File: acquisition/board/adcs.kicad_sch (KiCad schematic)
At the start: 107 parts, among them U1 AD9251, U2 XC7A50T-1FTG256C, U3 AD9251, U4 AD9251, U5 AD9251, U6 ICE40UP5K_QFN48

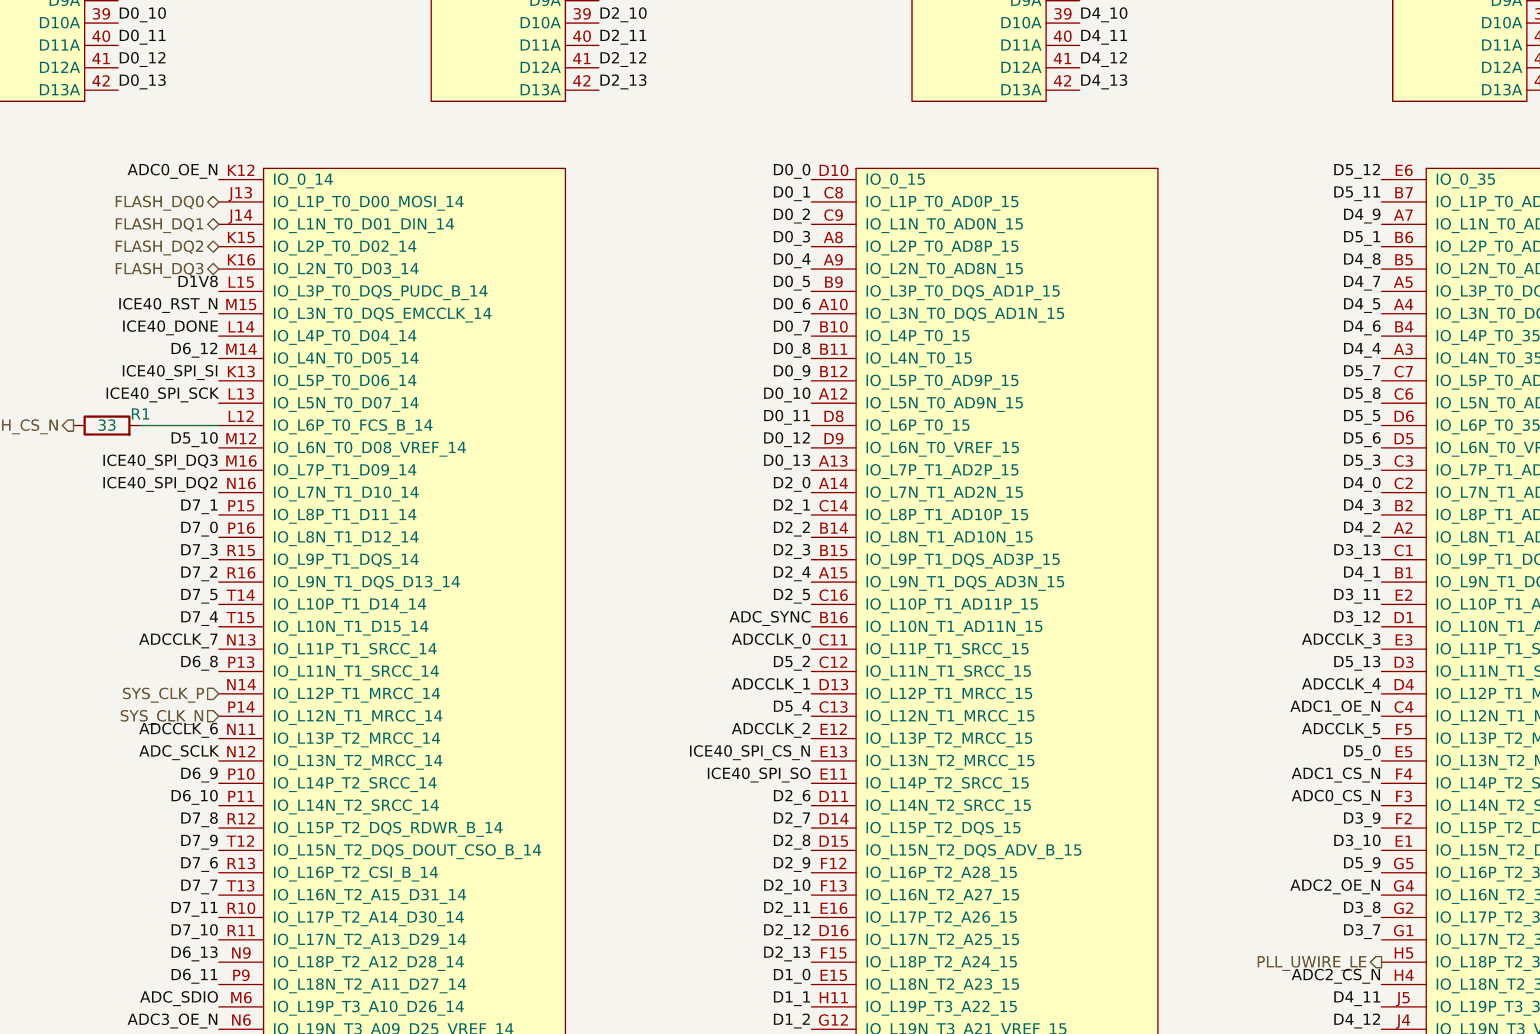
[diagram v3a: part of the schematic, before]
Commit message: Routed most of third ADC data bus
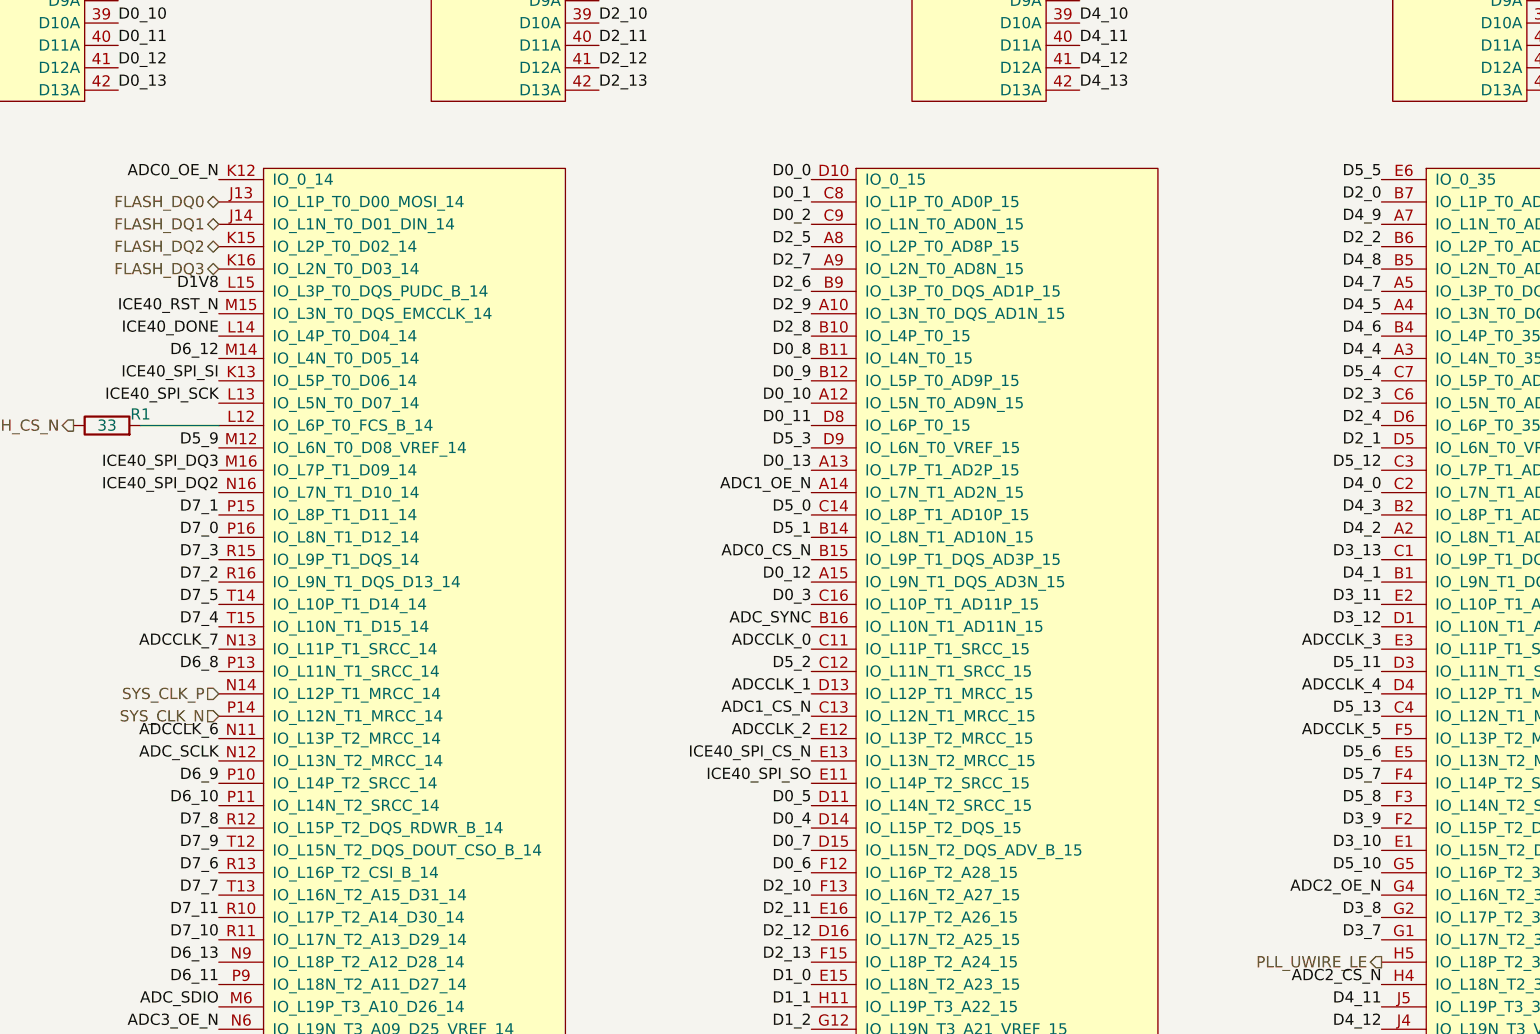
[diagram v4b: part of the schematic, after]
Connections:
- net ADC0_CS_N: now also U2.B15 (IO_L9P_T1_DQS_AD3P_15); no longer U2.F3 (IO_L14N_T2_SRCC_35)
- net ADC1_CS_N: now also U2.C13 (IO_L12N_T1_MRCC_15); no longer U2.F4 (IO_L14P_T2_SRCC_35)
- net ADC1_OE_N: now also U2.A14 (IO_L7N_T1_AD2N_15); no longer U2.C4 (IO_L12N_T1_MRCC_35)
- net D0_12: now also U2.A15 (IO_L9N_T1_DQS_AD3N_15); no longer U2.D9 (IO_L6N_T0_VREF_15)
- net D0_3: now also U2.C16 (IO_L10P_T1_AD11P_15); no longer U2.A8 (IO_L2P_T0_AD8P_15)
- net D0_4: now also U2.D14 (IO_L15P_T2_DQS_15); no longer U2.A9 (IO_L2N_T0_AD8N_15)
- net D0_5: now also U2.D11 (IO_L14N_T2_SRCC_15); no longer U2.B9 (IO_L3P_T0_DQS_AD1P_15)
- net D0_6: now also U2.F12 (IO_L16P_T2_A28_15); no longer U2.A10 (IO_L3N_T0_DQS_AD1N_15)
- net D0_7: now also U2.D15 (IO_L15N_T2_DQS_ADV_B_15); no longer U2.B10 (IO_L4P_T0_15)
- net D2_0: now also U2.B7 (IO_L1P_T0_AD4P_35); no longer U2.A14 (IO_L7N_T1_AD2N_15)
- net D2_1: now also U2.D5 (IO_L6N_T0_VREF_35); no longer U2.C14 (IO_L8P_T1_AD10P_15)
- net D2_2: now also U2.B6 (IO_L2P_T0_AD12P_35); no longer U2.B14 (IO_L8N_T1_AD10N_15)
- net D2_3: now also U2.C6 (IO_L5N_T0_AD13N_35); no longer U2.B15 (IO_L9P_T1_DQS_AD3P_15)
- net D2_4: now also U2.D6 (IO_L6P_T0_35); no longer U2.A15 (IO_L9N_T1_DQS_AD3N_15)
- net D2_5: now also U2.A8 (IO_L2P_T0_AD8P_15); no longer U2.C16 (IO_L10P_T1_AD11P_15)
- net D2_6: now also U2.B9 (IO_L3P_T0_DQS_AD1P_15); no longer U2.D11 (IO_L14N_T2_SRCC_15)
- net D2_7: now also U2.A9 (IO_L2N_T0_AD8N_15); no longer U2.D14 (IO_L15P_T2_DQS_15)
- net D2_8: now also U2.B10 (IO_L4P_T0_15); no longer U2.D15 (IO_L15N_T2_DQS_ADV_B_15)
- net D2_9: now also U2.A10 (IO_L3N_T0_DQS_AD1N_15); no longer U2.F12 (IO_L16P_T2_A28_15)
- net D5_0: now also U2.C14 (IO_L8P_T1_AD10P_15); no longer U2.E5 (IO_L13N_T2_MRCC_35)
- net D5_1: now also U2.B14 (IO_L8N_T1_AD10N_15); no longer U2.B6 (IO_L2P_T0_AD12P_35)
- net D5_10: now also U2.G5 (IO_L16P_T2_35); no longer U2.M12 (IO_L6N_T0_D08_VREF_14)
- net D5_11: now also U2.D3 (IO_L11N_T1_SRCC_35); no longer U2.B7 (IO_L1P_T0_AD4P_35)
- net D5_12: now also U2.C3 (IO_L7P_T1_AD6P_35); no longer U2.E6 (IO_0_35)
- net D5_13: now also U2.C4 (IO_L12N_T1_MRCC_35); no longer U2.D3 (IO_L11N_T1_SRCC_35)
- net D5_3: now also U2.D9 (IO_L6N_T0_VREF_15); no longer U2.C3 (IO_L7P_T1_AD6P_35)
- net D5_4: now also U2.C7 (IO_L5P_T0_AD13P_35); no longer U2.C13 (IO_L12N_T1_MRCC_15)
- net D5_5: now also U2.E6 (IO_0_35); no longer U2.D6 (IO_L6P_T0_35)
- net D5_6: now also U2.E5 (IO_L13N_T2_MRCC_35); no longer U2.D5 (IO_L6N_T0_VREF_35)
- net D5_7: now also U2.F4 (IO_L14P_T2_SRCC_35); no longer U2.C7 (IO_L5P_T0_AD13P_35)
- net D5_8: now also U2.F3 (IO_L14N_T2_SRCC_35); no longer U2.C6 (IO_L5N_T0_AD13N_35)
- net D5_9: now also U2.M12 (IO_L6N_T0_D08_VREF_14); no longer U2.G5 (IO_L16P_T2_35)
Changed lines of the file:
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@@
     (effects (font (size 1.27 1.27)) (justify right bottom))
   )
-  (label "D2_0" (at 130.81 182.88 180)
+  (label "D2_0" (at 195.58 149.86 180)
     (effects (font (size 1.27 1.27)) (justify right bottom))
   )
@@
     (effects (font (size 1.27 1.27)) (justify right bottom))
   )
-  (label "ADC0_CS_N" (at 195.58 218.44 180)
+  (label "ADC0_CS_N" (at 130.81 190.5 180)
     (effects (font (size 1.27 1.27)) (justify right bottom))
   )
@@
     (effects (font (size 1.27 1.27)) (justify right bottom))
   )
-  (label "D2_5" (at 130.81 195.58 180)
+  (label "D2_5" (at 130.81 154.94 180)
     (effects (font (size 1.27 1.27)) (justify right bottom))
   )
@@
     (effects (font (size 1.27 1.27)) (justify right bottom))
   )
-  (label "D2_8" (at 130.81 223.52 180)
+  (label "D2_8" (at 130.81 165.1 180)
     (effects (font (size 1.27 1.27)) (justify right bottom))
   )
@@
     (effects (font (size 1.27 1.27)) (justify right bottom))
   )
-  (label "D5_1" (at 195.58 154.94 180)
-    (effects (font (size 1.27 1.27)) (justify right bottom))
-  )
-  (label "D2_6" (at 130.81 218.44 180)
-    (effects (font (size 1.27 1.27)) (justify right bottom))
-  )
-  (label "ADC1_CS_N" (at 195.58 215.9 180)
+  (label "D5_1" (at 130.81 187.96 180)
+    (effects (font (size 1.27 1.27)) (justify right bottom))
+  )
+  (label "D2_6" (at 130.81 160.02 180)
+    (effects (font (size 1.27 1.27)) (justify right bottom))
+  )
+  (label "ADC1_CS_N" (at 130.81 208.28 180)
     (effects (font (size 1.27 1.27)) (justify right bottom))
   )
@@
     (effects (font (size 1.27 1.27)) (justify left bottom))
   )
-  (label "D0_6" (at 130.81 162.56 180)
+  (label "D0_6" (at 130.81 226.06 180)
     (effects (font (size 1.27 1.27)) (justify right bottom))
   )
@@
     (effects (font (size 1.27 1.27)) (justify right bottom))
   )
-  (label "D0_7" (at 130.81 165.1 180)
+  (label "D0_7" (at 130.81 223.52 180)
     (effects (font (size 1.27 1.27)) (justify right bottom))
   )
@@
     (effects (font (size 1.27 1.27)) (justify left bottom))
   )
-  (label "D2_2" (at 130.81 187.96 180)
+  (label "D2_2" (at 195.58 154.94 180)
     (effects (font (size 1.27 1.27)) (justify right bottom))
   )
@@
     (effects (font (size 1.27 1.27)) (justify left bottom))
   )
-  (label "D5_11" (at 195.58 149.86 180)
+  (label "D5_11" (at 195.58 203.2 180)
     (effects (font (size 1.27 1.27)) (justify right bottom))
   )
@@
     (effects (font (size 1.27 1.27)) (justify right bottom))
   )
-  (label "D5_9" (at 195.58 226.06 180)
+  (label "D5_9" (at 63.5 177.8 180)
     (effects (font (size 1.27 1.27)) (justify right bottom))
   )
@@
     (effects (font (size 1.27 1.27)) (justify right bottom))
   )
-  (label "D2_4" (at 130.81 193.04 180)
+  (label "D2_4" (at 195.58 175.26 180)
     (effects (font (size 1.27 1.27)) (justify right bottom))
   )
@@
     (effects (font (size 1.27 1.27)) (justify right bottom))
   )
-  (label "D5_3" (at 195.58 180.34 180)
+  (label "D5_3" (at 130.81 177.8 180)
     (effects (font (size 1.27 1.27)) (justify right bottom))
   )
@@
     (effects (font (size 1.27 1.27)) (justify right bottom))
   )
-  (label "D5_4" (at 130.81 208.28 180)
+  (label "D5_4" (at 195.58 170.18 180)
     (effects (font (size 1.27 1.27)) (justify right bottom))
   )
@@
     (effects (font (size 1.27 1.27)) (justify right bottom))
   )
-  (label "D2_1" (at 130.81 185.42 180)
+  (label "D2_1" (at 195.58 177.8 180)
     (effects (font (size 1.27 1.27)) (justify right bottom))
   )
@@
     (effects (font (size 1.27 1.27)) (justify left bottom))
   )
-  (label "D0_5" (at 130.81 160.02 180)
+  (label "D0_5" (at 130.81 218.44 180)
     (effects (font (size 1.27 1.27)) (justify right bottom))
   )
@@
     (effects (font (size 1.27 1.27)) (justify left bottom))
   )
-  (label "D2_9" (at 130.81 226.06 180)
+  (label "D2_9" (at 130.81 162.56 180)
     (effects (font (size 1.27 1.27)) (justify right bottom))
   )
@@
     (effects (font (size 1.27 1.27)) (justify right bottom))
   )
-  (label "D0_3" (at 130.81 154.94 180)
+  (label "D0_3" (at 130.81 195.58 180)
     (effects (font (size 1.27 1.27)) (justify right bottom))
   )
@@
     (effects (font (size 1.27 1.27)) (justify right bottom))
   )
-  (label "D5_0" (at 195.58 213.36 180)
+  (label "D5_0" (at 130.81 185.42 180)
     (effects (font (size 1.27 1.27)) (justify right bottom))
   )
@@
     (effects (font (size 1.27 1.27)) (justify right bottom))
   )
-  (label "D0_12" (at 130.81 177.8 180)
+  (label "D0_12" (at 130.81 193.04 180)
     (effects (font (size 1.27 1.27)) (justify right bottom))
   )
@@
     (effects (font (size 1.27 1.27)) (justify right bottom))
   )
-  (label "D2_7" (at 130.81 220.98 180)
+  (label "D2_7" (at 130.81 157.48 180)
     (effects (font (size 1.27 1.27)) (justify right bottom))
   )
@@
     (effects (font (size 1.27 1.27)) (justify right bottom))
   )
-  (label "D5_12" (at 195.58 147.32 180)
+  (label "D5_12" (at 195.58 180.34 180)
     (effects (font (size 1.27 1.27)) (justify right bottom))
   )
@@
     (effects (font (size 1.27 1.27)) (justify right bottom))
   )
-  (label "D5_7" (at 195.58 170.18 180)
+  (label "D5_7" (at 195.58 215.9 180)
     (effects (font (size 1.27 1.27)) (justify right bottom))
   )
@@
     (effects (font (size 1.27 1.27)) (justify left bottom))
   )
-  (label "D5_6" (at 195.58 177.8 180)
+  (label "D5_6" (at 195.58 213.36 180)
     (effects (font (size 1.27 1.27)) (justify right bottom))
   )
@@
     (effects (font (size 1.27 1.27)) (justify left bottom))
   )
-  (label "D2_3" (at 130.81 190.5 180)
-    (effects (font (size 1.27 1.27)) (justify right bottom))
-  )
-  (label "D5_10" (at 63.5 177.8 180)
+  (label "D2_3" (at 195.58 172.72 180)
+    (effects (font (size 1.27 1.27)) (justify right bottom))
+  )
+  (label "D5_10" (at 195.58 226.06 180)
     (effects (font (size 1.27 1.27)) (justify right bottom))
   )
@@
     (effects (font (size 1.27 1.27)) (justify right bottom))
   )
-  (label "D5_8" (at 195.58 172.72 180)
+  (label "D5_8" (at 195.58 218.44 180)
     (effects (font (size 1.27 1.27)) (justify right bottom))
   )
@@
     (effects (font (size 1.27 1.27)) (justify right bottom))
   )
-  (label "D0_4" (at 130.81 157.48 180)
+  (label "D0_4" (at 130.81 220.98 180)
     (effects (font (size 1.27 1.27)) (justify right bottom))
   )
@@
     (effects (font (size 1.27 1.27)) (justify right bottom))
   )
-  (label "ADC1_OE_N" (at 195.58 208.28 180)
+  (label "ADC1_OE_N" (at 130.81 182.88 180)
     (effects (font (size 1.27 1.27)) (justify right bottom))
   )
@@
     (effects (font (size 1.27 1.27)) (justify right bottom))
   )
-  (label "D5_13" (at 195.58 203.2 180)
+  (label "D5_13" (at 195.58 208.28 180)
     (effects (font (size 1.27 1.27)) (justify right bottom))
   )
@@
     (effects (font (size 1.27 1.27)) (justify right bottom))
   )
-  (label "D5_5" (at 195.58 175.26 180)
-    (effects (font (size 1.27 1.27)) (justify right bottom))
-  )
+  (label "D5_5" (at 195.58 147.32 180)
+    (effects (font (size 1.27 1.27)) (justify right bottom))
+  )
